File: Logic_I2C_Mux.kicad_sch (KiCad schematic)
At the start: 12 parts, among them U801 PCA9546ARGVR

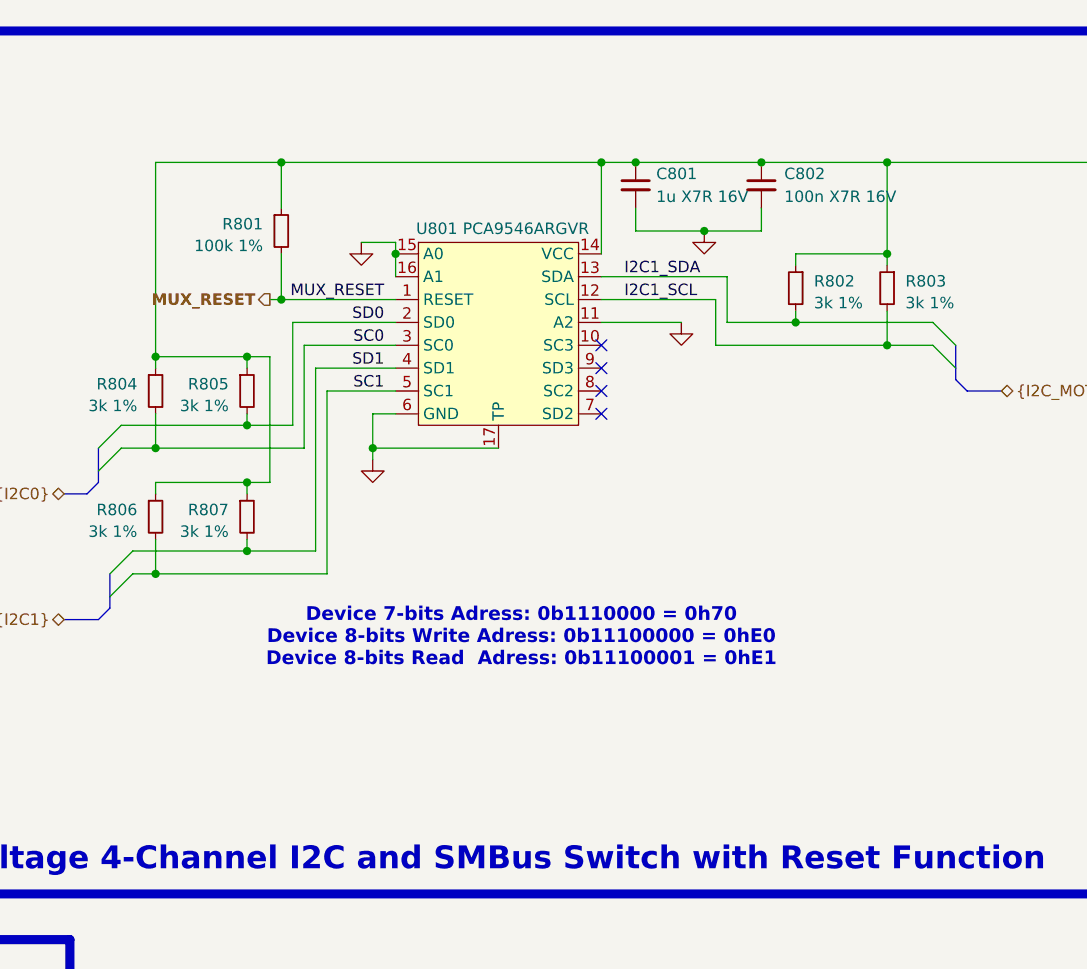
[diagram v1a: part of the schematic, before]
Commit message: Added PCB frame for assembly, almost finished auto-review, only MCU and motors left
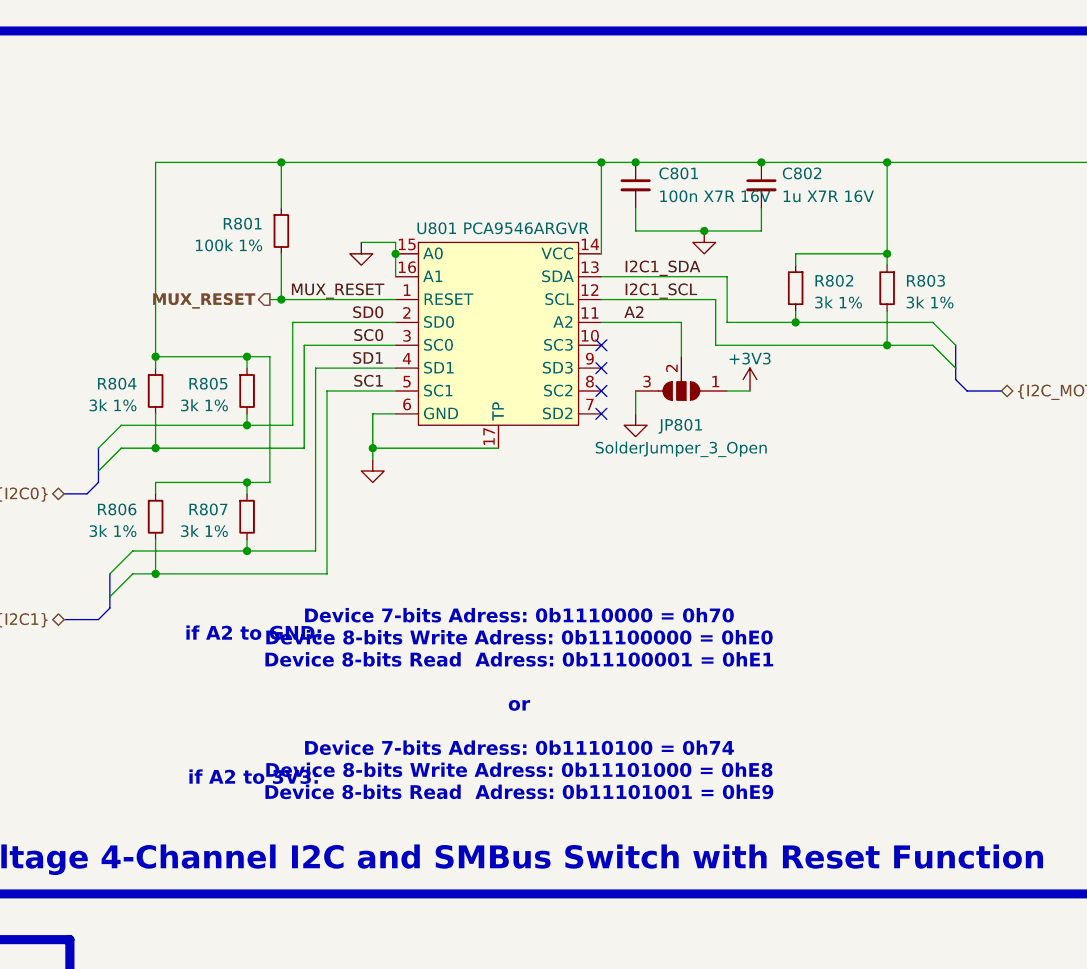
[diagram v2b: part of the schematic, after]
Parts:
- added JP801: SolderJumper_3_Open, 0_Plume:SolderJumper-3_P1.3mm_Open_RoundedPad1.0x1.5mm_clean, symbol Jumper:SolderJumper_3_Open
- TP801: footprint 0_Plume:TestPoint_Pad_D0.5mm_Back -> 0_Plume:TestPoint_Pad_D0.5mm_Front
- renumbered C802 to C801, C801 to C802
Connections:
- net +3V3: now also JP801.1 (A)
- net GND: now also JP801.3 (B); no longer U801.11 (A2)
- new net A2: JP801.2 (C), U801.11 (A2)
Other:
- note added: "Device 7-bits Adress: 0b1110000 = 0h70 Device 8-bits Write Adress: 0b11100000 = 0hE0 Device 8-bits Read Adress: 0b11100001 = 0hE1 or Device 7-bits Adress: 0b1110100 = 0h74 Device 8-bits Write Adress: 0b11101000 = 0hE8 Device 8-bits Read Adress: 0b11101001 = 0hE9"
- note added: "if A2 to 3V3:"
- note added: "if A2 to GND:"
- note removed: "Device 7-bits Adress: 0b1110000 = 0h70 Device 8-bits Write Adress: 0b11100000 = 0hE0 Device 8-bits Read Adress: 0b11100001 = 0hE1"
- moved on the sheet: C801, C802

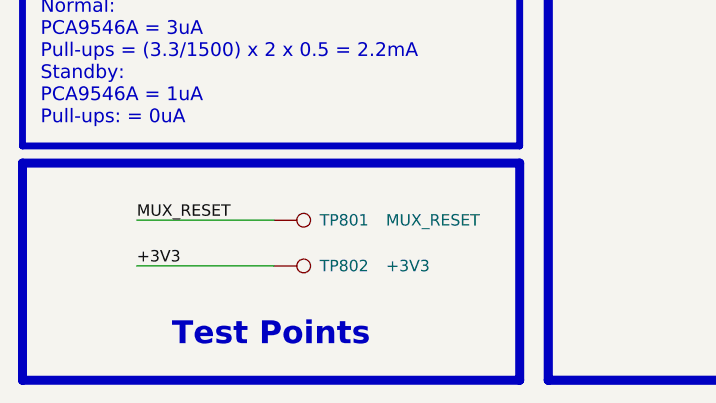
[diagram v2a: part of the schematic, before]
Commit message: Checked everything, corrected footprints, cleaned routing, should be ready to order
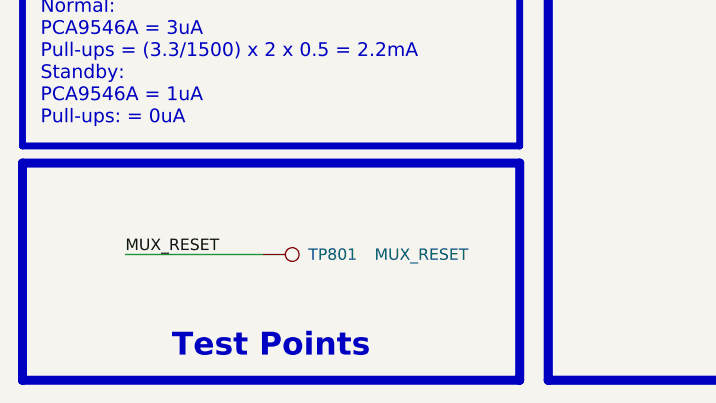
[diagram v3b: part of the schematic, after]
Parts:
- removed TP802: +3V3, 0_Plume:TestPoint_Pad_D0.5mm_Back, symbol Connector:TestPoint
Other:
- moved on the sheet: TP801
